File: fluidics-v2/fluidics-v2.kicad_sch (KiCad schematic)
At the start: 20 parts, among them J1 PJ-063AH, J10 0705430001, J11 0705430001, J12 87832-1010, J13 87832-1010, J14 87832-1010, J15 87832-1010, J16 87832-1010, J2 1860280, J3 0533980671, J4 0533980671, J6 A-DS_15_A_KG-T4S, J7 0705430001, J8 0705430001, J9 0705430001, U1 Teensy4.1

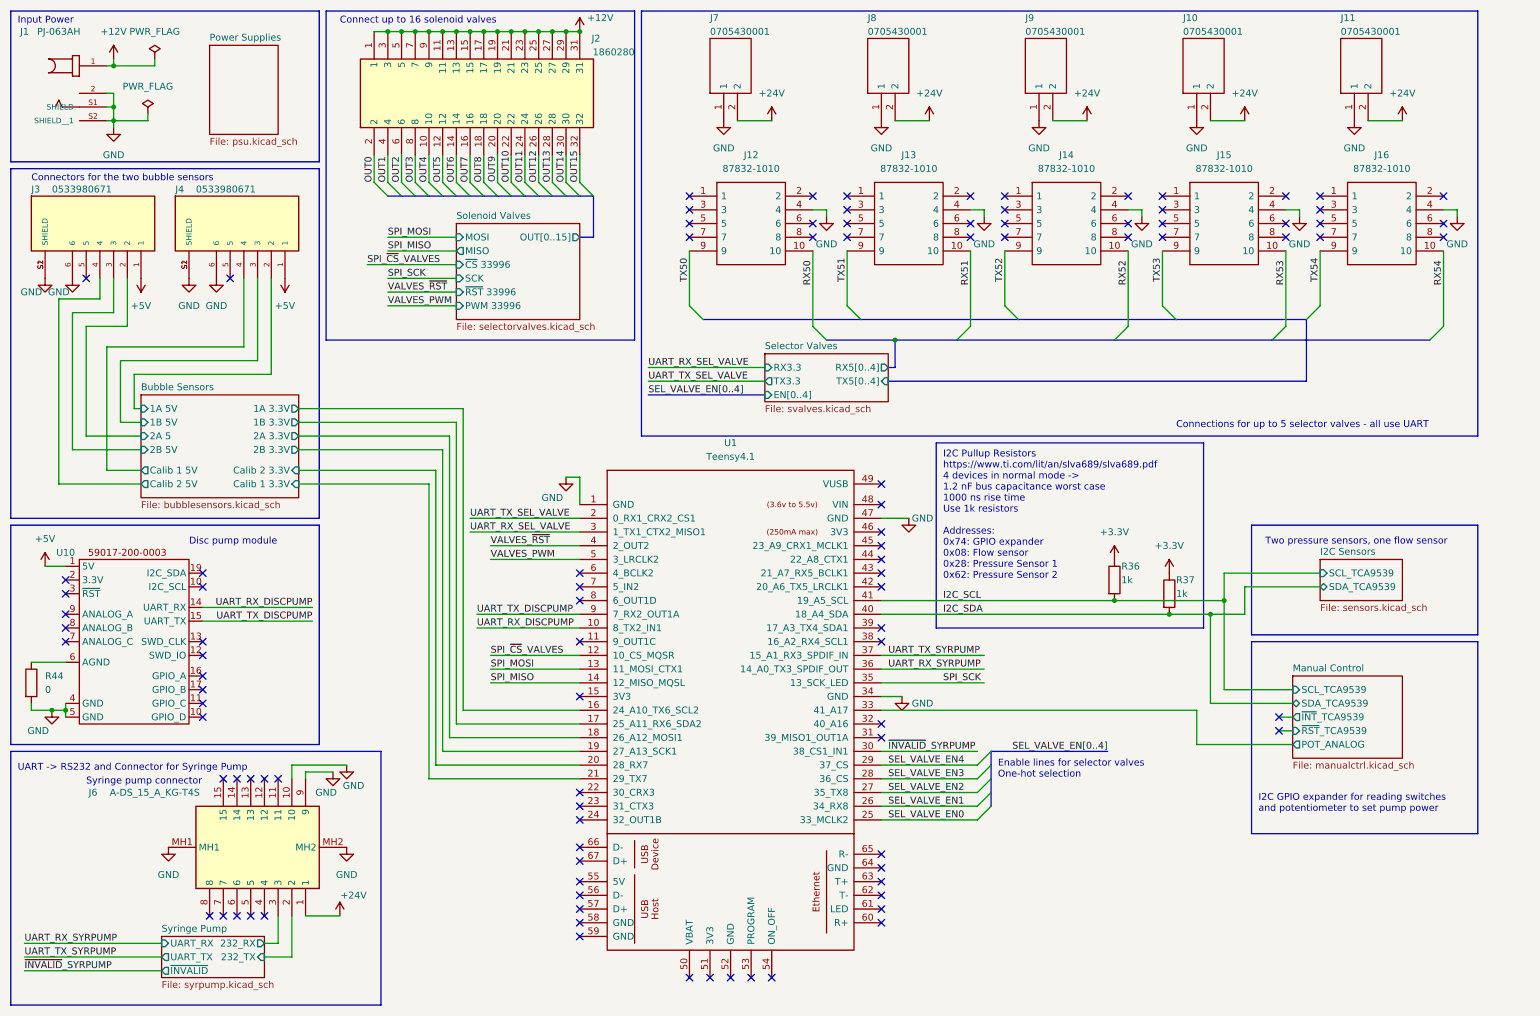
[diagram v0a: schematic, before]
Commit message: added footprints and mounting holes, cleaned up some sheets
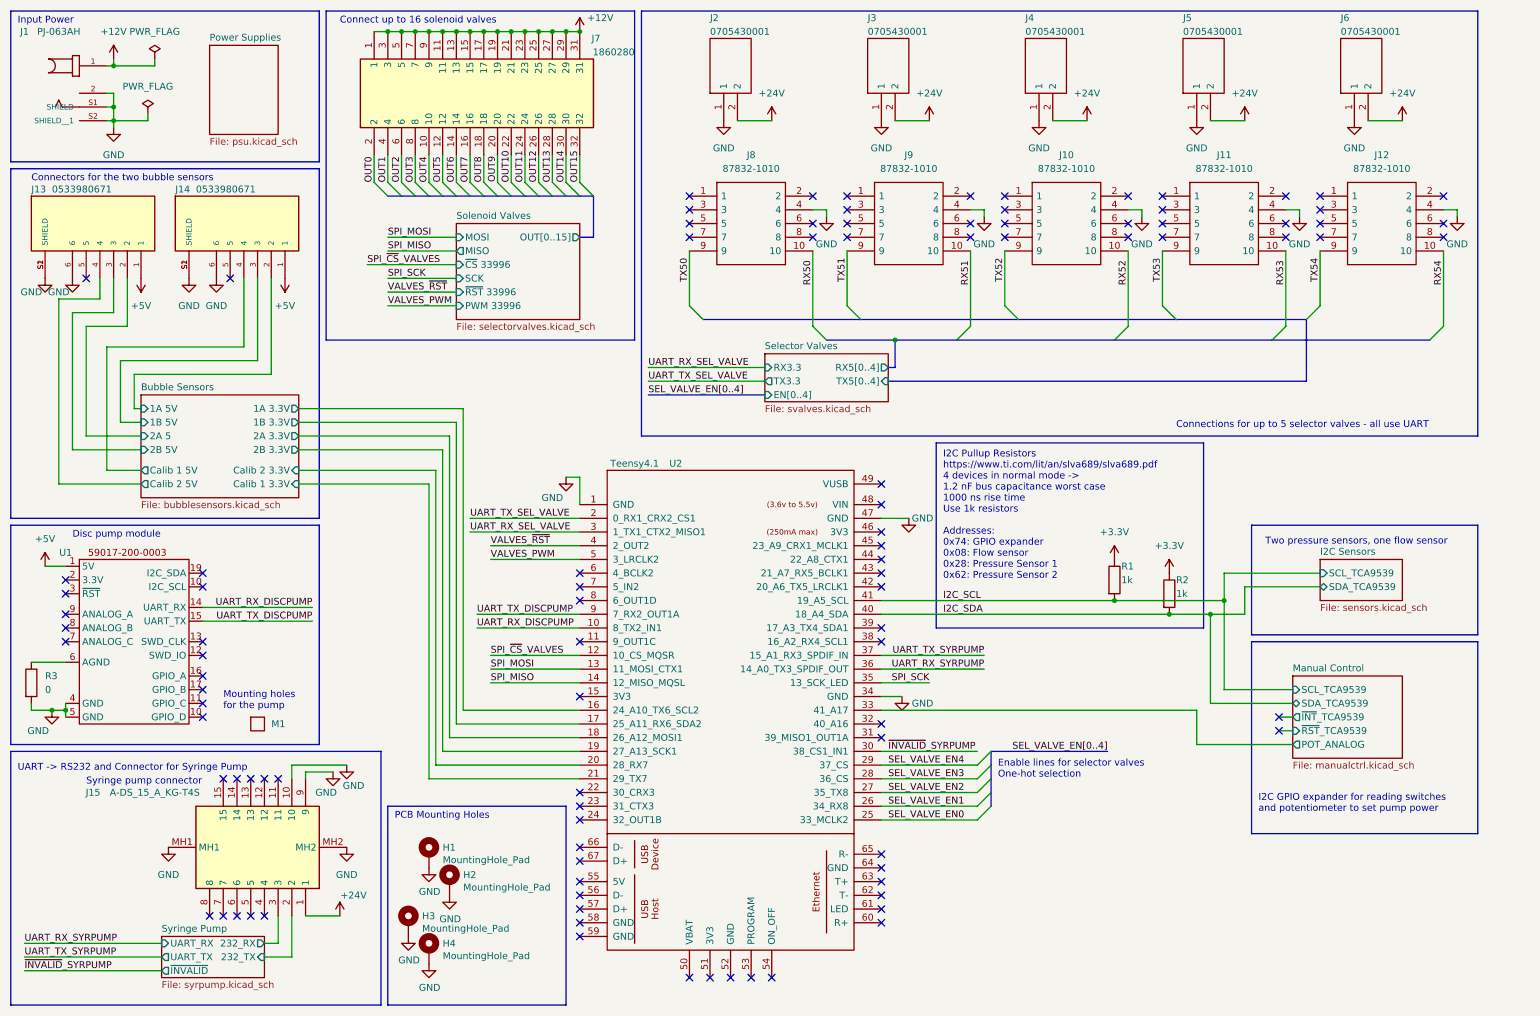
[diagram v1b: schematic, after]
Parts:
- added H1, H2, H3, H4: MountingHole_Pad, MountingHole:MountingHole_3.2mm_M3_Pad_Via, symbol Mechanical:MountingHole_Pad
- added M1: ~, TTP Ventus:Pump Mount, symbol ttp:Pump_Mounting
- renumbered J14 to J10, J15 to J11, J16 to J12, J3 to J13, J4 to J14, J6 to J15, J7 to J2, J8 to J3, J9 to J4, J10 to J5, J11 to J6, J2 to J7, J12 to J8, J13 to J9, R36 to R1, R37 to R2, R44 to R3, U10 to U1, U1 to U2
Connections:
- net GND: now also H1.1, H2.1, H3.1, H4.1
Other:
- note added: "Mounting holes for the pump"
- note added: "PCB Mounting Holes"
